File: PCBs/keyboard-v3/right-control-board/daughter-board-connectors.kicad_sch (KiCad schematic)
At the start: 0 parts

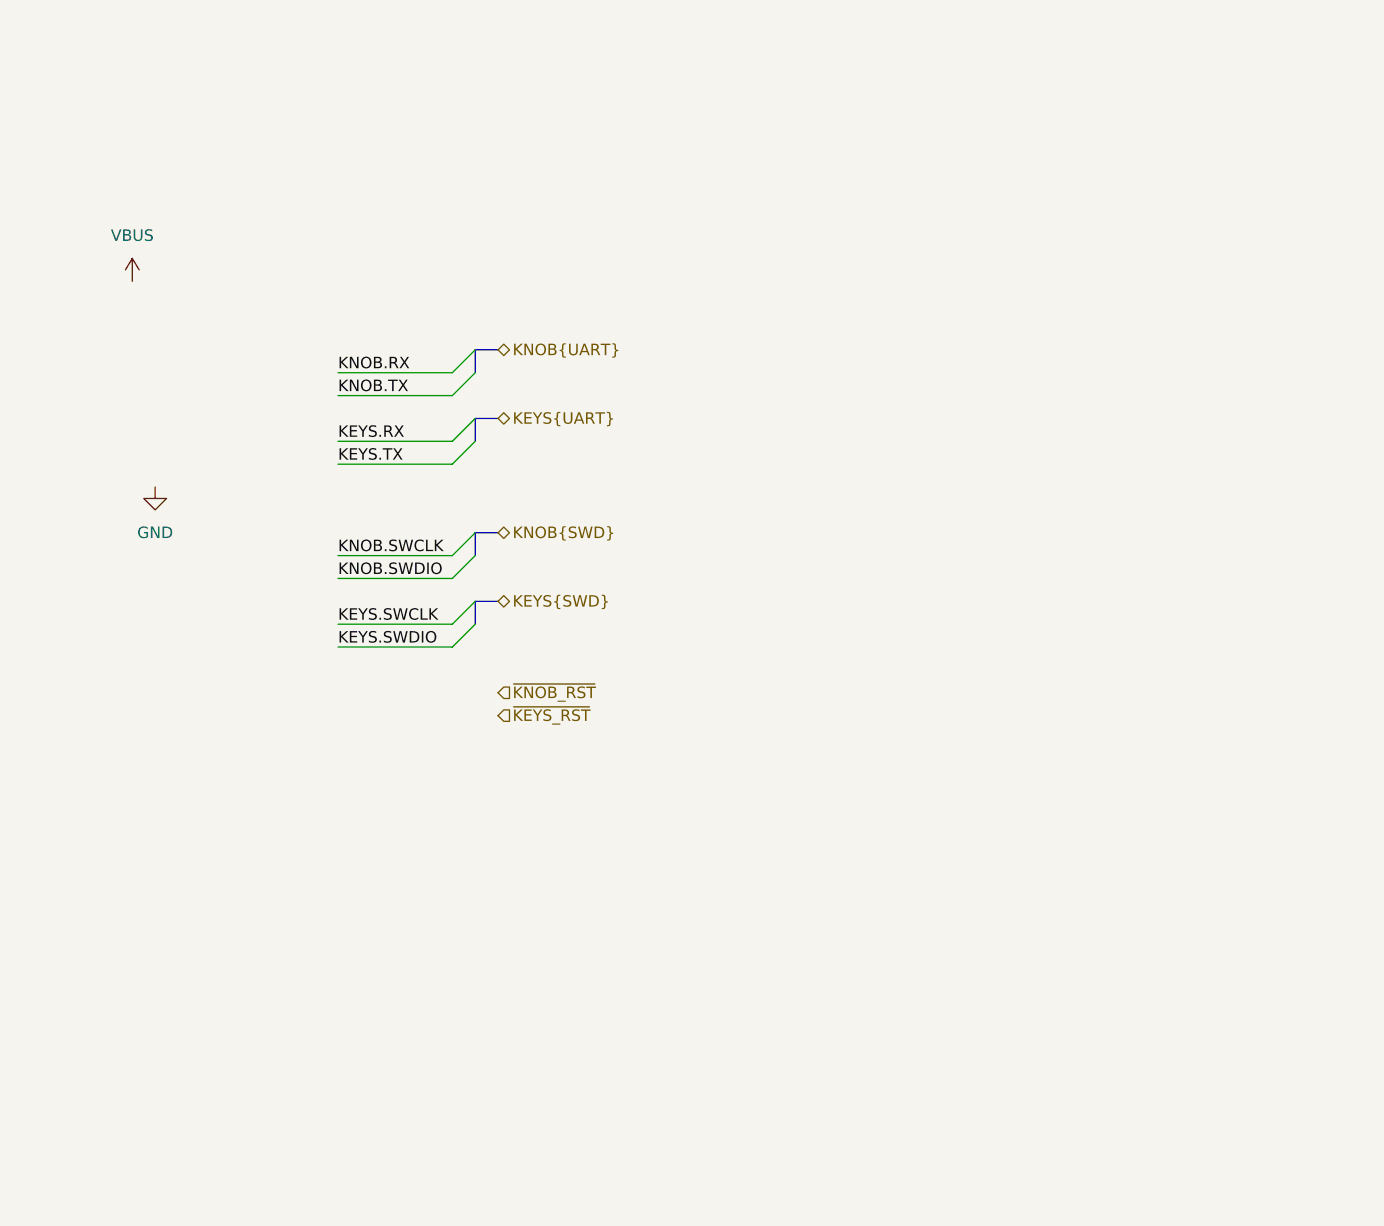
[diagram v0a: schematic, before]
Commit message: Key board schematic done and layout half done
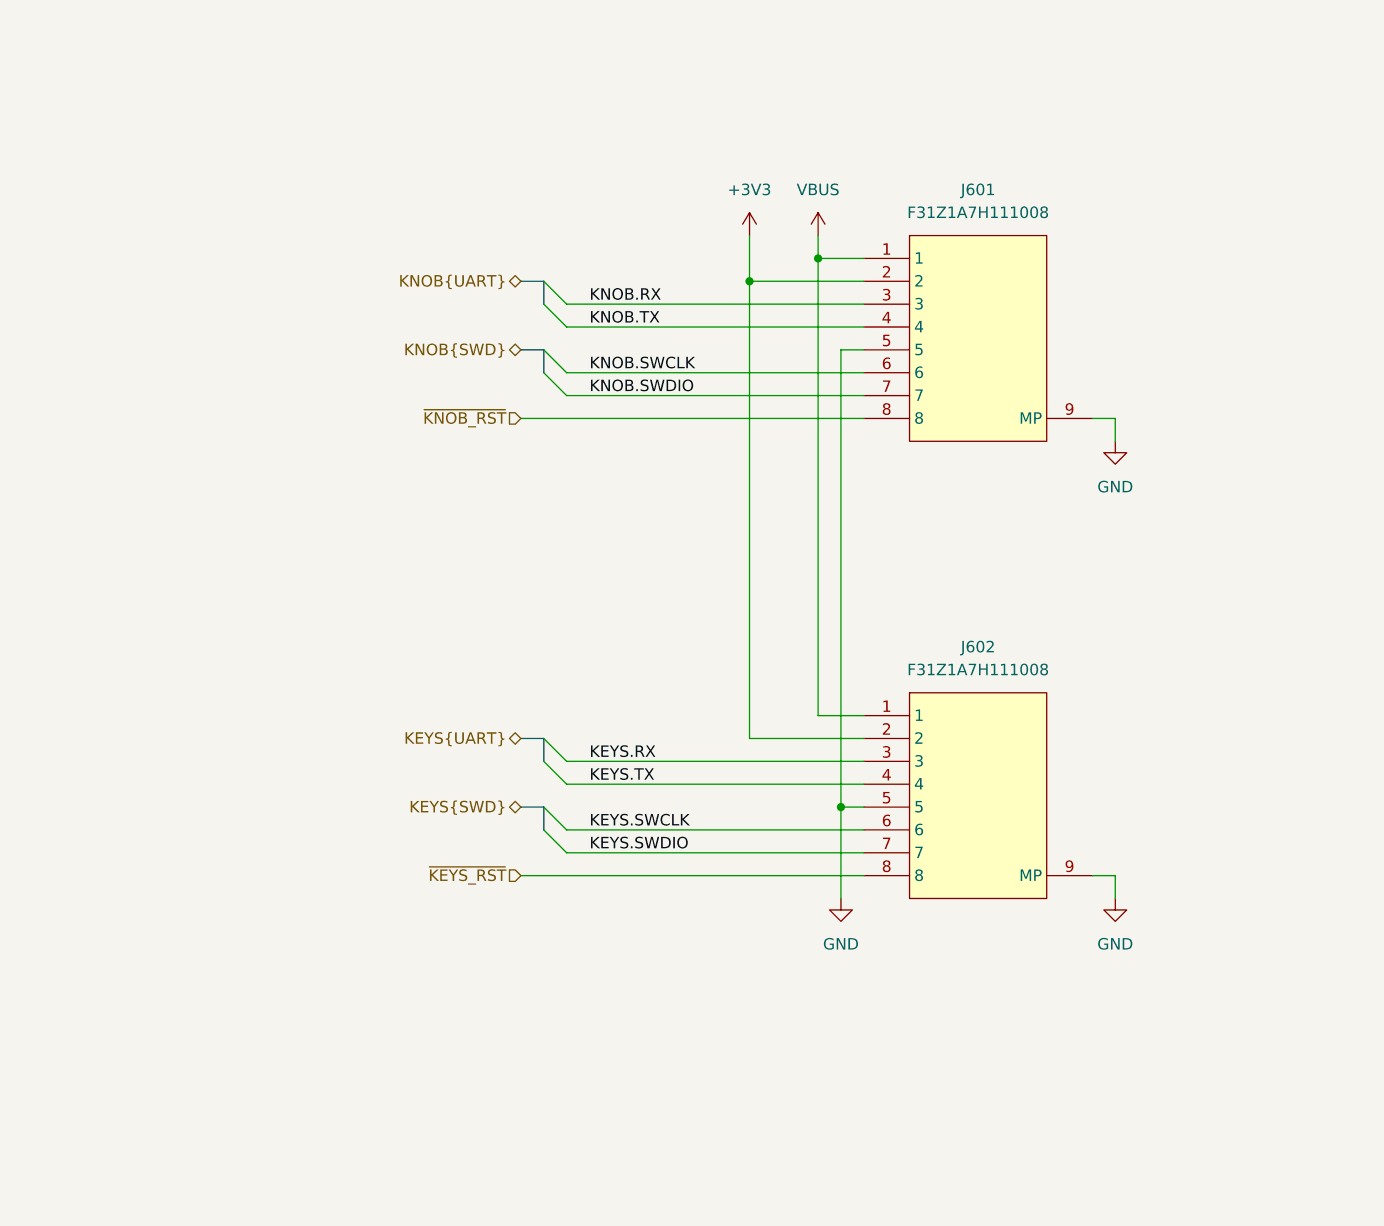
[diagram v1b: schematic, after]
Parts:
- added J601, J602: F31Z1A7H111008, project_footprints:F31Z1A7H111008, symbol CONN-FPC:F31Z1A7H111008
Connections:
- net GND: now also J601.10 (MP), J601.11 (MP), J601.12 (MP), J601.5, J601.9 (MP), J602.10 (MP), J602.11 (MP), J602.12 (MP), J602.5, J602.9 (MP)
- net KEYS.RX: now also J602.3
- net KEYS.SWCLK: now also J602.6
- net KEYS.SWDIO: now also J602.7
- net KEYS.TX: now also J602.4
- net KNOB.RX: now also J601.3
- net KNOB.SWCLK: now also J601.6
- net KNOB.SWDIO: now also J601.7
- net KNOB.TX: now also J601.4
- net VBUS: now also J601.1, J602.1
- net ~{KEYS_RST}: now also J602.8
- net ~{KNOB_RST}: now also J601.8
- new net +3V3: J601.2, J602.2

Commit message: Added debug-breakout board, progress on right side schematics & layout
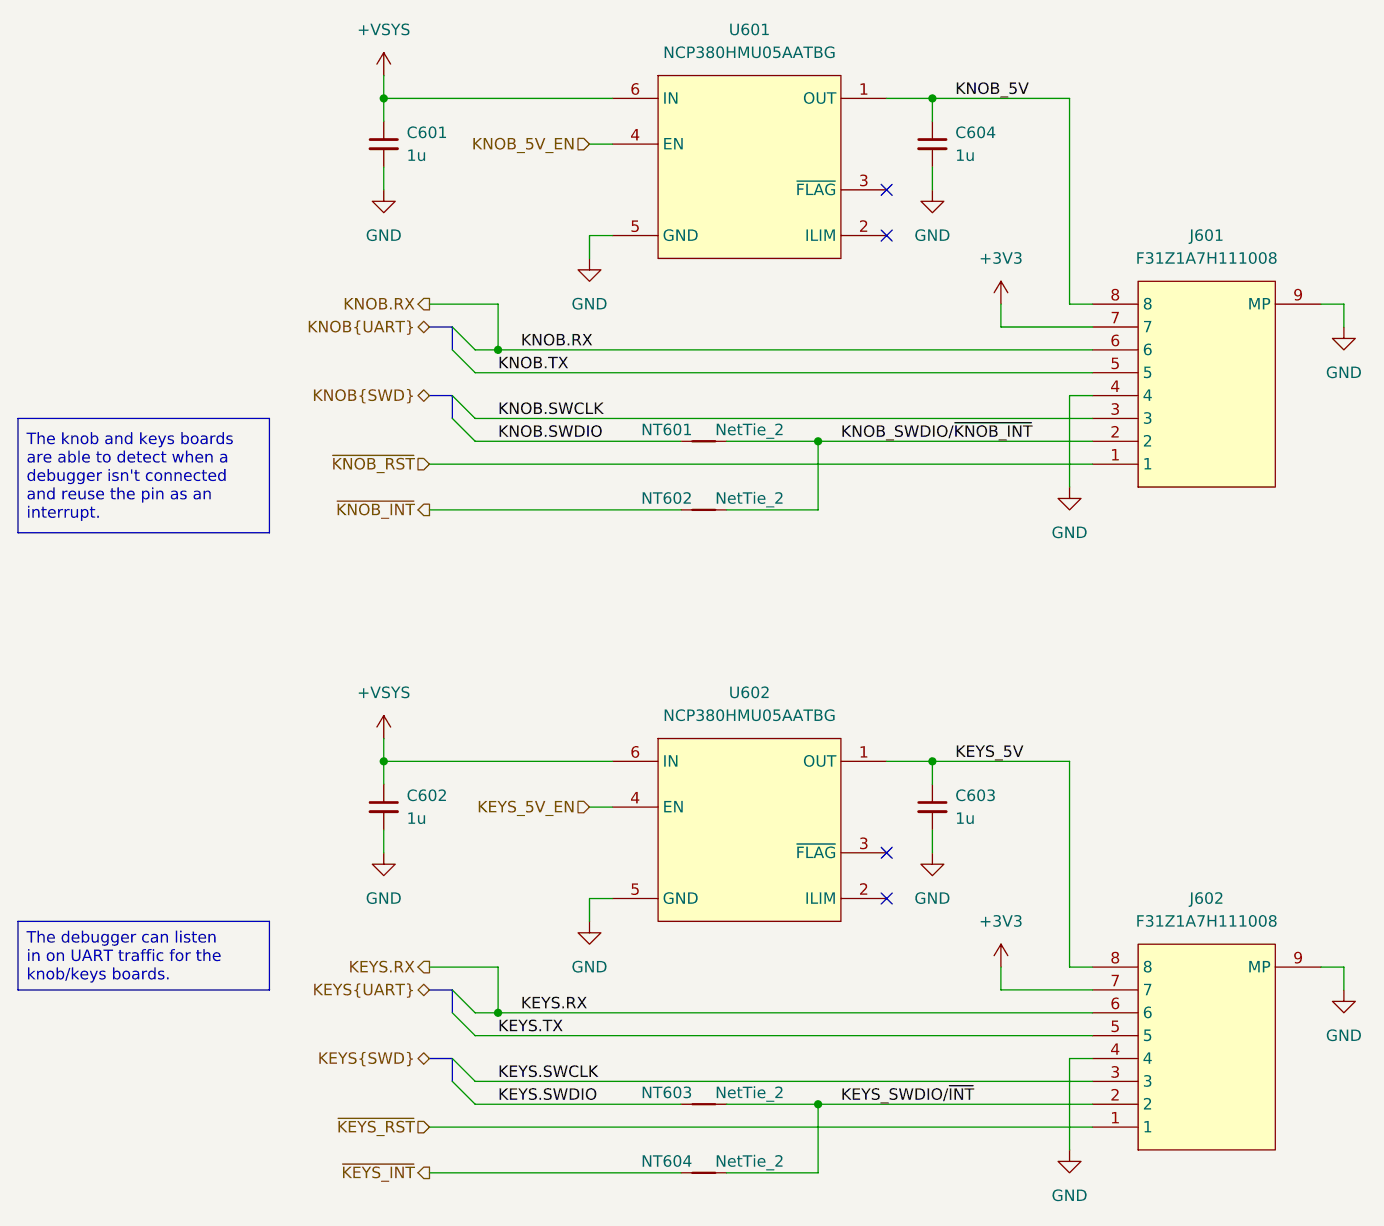
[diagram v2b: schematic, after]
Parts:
- added C601, C602, C603, C604: 1u, project_footprints:C_0402, symbol DEV:C_SMALL
- added NT601, NT602, NT603, NT604: NetTie_2, project_footprints:NetTie-2_SMD_Pad0.15mm, symbol Device:NetTie_2
- added U601, U602: NCP380HMU05AATBG, project_footprints:SON65P200X200X55-7N, symbol PWR-SWCH:NCP380HMU05AATBG
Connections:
- net +3V3: now also J601.7, J602.7; no longer J601.2, J602.2
- net GND: now also J601.4, J602.4, C601.2, C602.2, C603.2, C604.2, U601.5 (GND), U601.7 (GND), U602.5 (GND), U602.7 (GND); no longer J601.5, J602.5
- net KEYS.RX: now also J602.6; no longer J602.3
- net KEYS.SWCLK: now also J602.3; no longer J602.6
- net KEYS.SWDIO: now also NT603.1; no longer J602.7
- net KEYS.TX: now also J602.5; no longer J602.4
- net KNOB.RX: now also J601.6; no longer J601.3
- net KNOB.SWCLK: now also J601.3; no longer J601.6
- net KNOB.SWDIO: now also NT601.1; no longer J601.7
- net KNOB.TX: now also J601.5; no longer J601.4
- net ~{KEYS_RST}: now also J602.1; no longer J602.8
- net ~{KNOB_RST}: now also J601.1; no longer J601.8
- removed net VBUS: J601.1, J602.1
- new net +VSYS: C601.1, C602.1, U601.6 (IN), U602.6 (IN)
- new net KEYS_5V: C603.1, J602.8, U602.1 (OUT)
- new net KEYS_5V_EN: U602.4 (EN)
- new net KEYS_SWDIO/~{INT}: J602.2, NT603.2, NT604.2
- new net KNOB_5V: C604.1, J601.8, U601.1 (OUT)
- new net KNOB_5V_EN: U601.4 (EN)
- new net KNOB_SWDIO/~{KNOB_INT}: J601.2, NT601.2, NT602.2
- new net ~{KEYS_INT}: NT604.1
- new net ~{KNOB_INT}: NT602.1
- no-connect marks 0 -> 4
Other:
- moved on the sheet: J601, J602

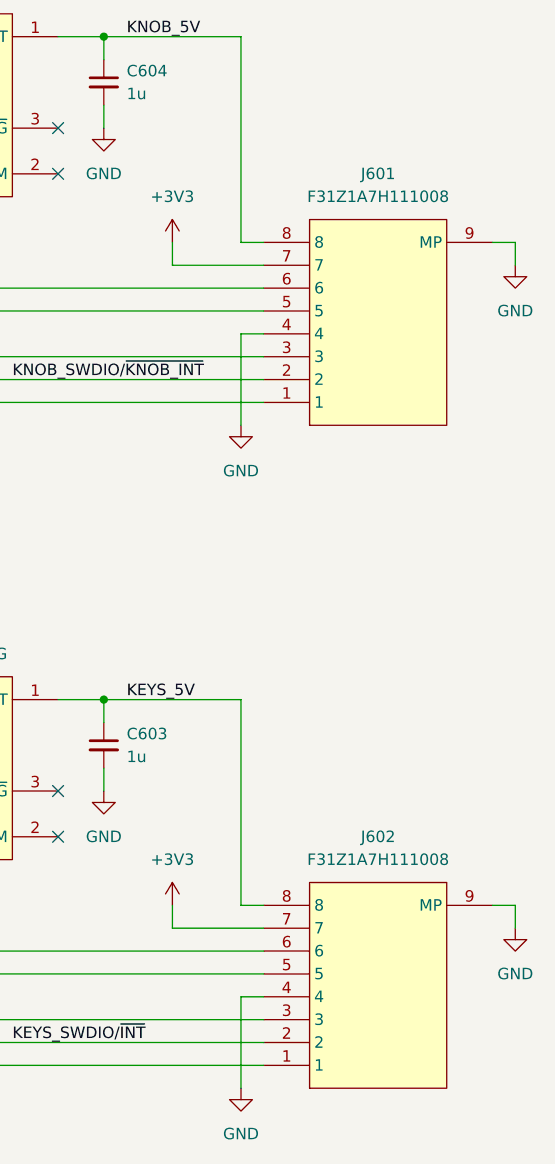
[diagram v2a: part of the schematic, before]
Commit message: Right control board placement and schematic done
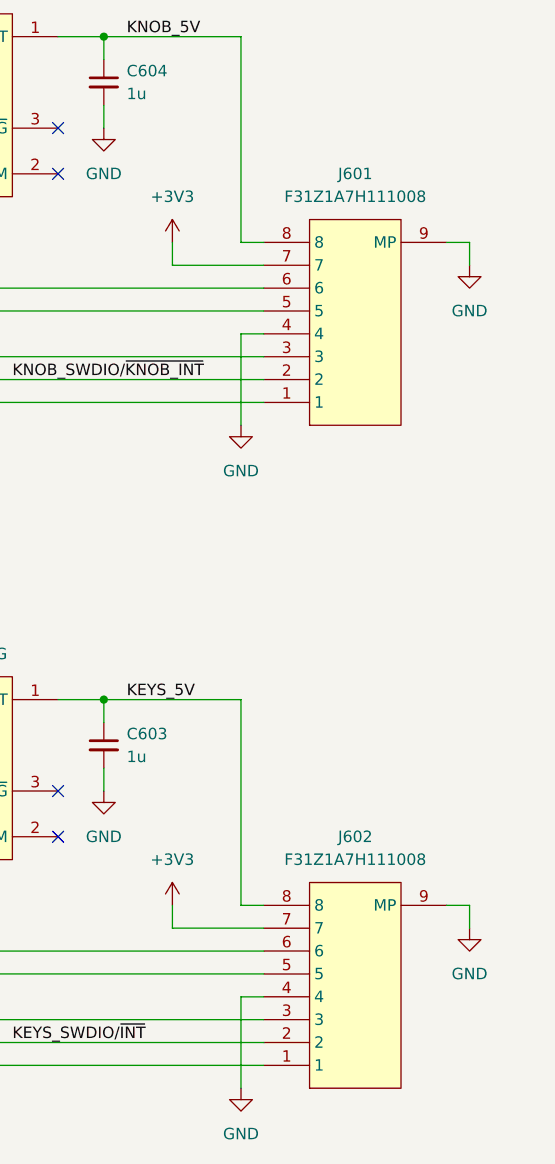
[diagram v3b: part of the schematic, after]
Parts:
- J601, J602: symbol CONN-FPC:F31Z1A7H111008 -> CONN-FPC:F31Z-1A7H1-11008
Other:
- moved on the sheet: J601, J602
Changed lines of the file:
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@@
 	(wire
 		(pts
-			(xy 218.44 58.42) (xy 218.44 60.96)
+			(xy 213.36 58.42) (xy 213.36 60.96)
 		)
 		(stroke
@@
 	(wire
 		(pts
-			(xy 215.9 58.42) (xy 218.44 58.42)
+			(xy 210.82 58.42) (xy 213.36 58.42)
 		)
 		(stroke
@@
 	(wire
 		(pts
-			(xy 215.9 132.08) (xy 218.44 132.08)
+			(xy 210.82 132.08) (xy 213.36 132.08)
 		)
 		(stroke
@@
 	(wire
 		(pts
-			(xy 218.44 134.62) (xy 218.44 132.08)
+			(xy 213.36 134.62) (xy 213.36 132.08)
 		)
 		(stroke
@@
 	(symbol
 		(lib_id "power:GND")
-		(at 218.44 60.96 0)
+		(at 213.36 60.96 0)
 		(unit 1)
 		(exclude_from_sim no)
@@
 		(fields_autoplaced yes)
 		(property "Reference" "#PWR0603"
-			(at 218.44 67.31 0)
+			(at 213.36 67.31 0)
 			(effects
 				(font
@@
 		)
 		(property "Value" "GND"
-			(at 218.44 66.04 0)
+			(at 213.36 66.04 0)
 			(effects
 				(font
@@
 		)
 		(property "Footprint" ""
-			(at 218.44 60.96 0)
+			(at 213.36 60.96 0)
 			(effects
 				(font
@@
 		)
 		(property "Datasheet" ""
-			(at 218.44 60.96 0)
+			(at 213.36 60.96 0)
 			(effects
 				(font
@@
 		)
 		(property "Description" ""
-			(at 218.44 60.96 0)
+			(at 213.36 60.96 0)
 			(effects
 				(font
@@
 	)
 	(symbol
-		(lib_id "CONN-FPC:F31Z1A7H111008")
-		(at 203.2 78.74 0)
+		(lib_id "CONN-FPC:F31Z-1A7H1-11008")
+		(at 200.66 78.74 0)
 		(mirror x)
 		(unit 1)
@@
 		(dnp no)
 		(property "Reference" "J601"
-			(at 203.2 50.8 0)
+			(at 200.66 50.8 0)
 			(effects
 				(font
@@
 		)
 		(property "Value" "F31Z1A7H111008"
-			(at 203.2 53.34 0)
+			(at 200.66 53.34 0)
 			(effects
 				(font
@@
 		)
 		(property "Footprint" "project_footprints:F31Z1A7H111008"
-			(at 203.2 50.8 0)
+			(at 200.66 50.8 0)
 			(effects
 				(font
@@
 		)
 		(property "Datasheet" "https://cdn.amphenol-cs.com/media/wysiwyg/files/drawing/f31z-f31w.pdf"
-			(at 203.2 48.26 0)
+			(at 200.66 48.26 0)
 			(effects
 				(font
@@
 		)
 		(property "Description" "Flex Connector, 0.50mm Pitch, Height 4.25mm, Vertical, Slider type, ZIF, 8 position, With MYLAR"
-			(at 203.2 53.34 0)
+			(at 200.66 53.34 0)
 			(effects
 				(font
@@
 		)
 		(property "Height" "4.45"
-			(at 203.2 45.72 0)
+			(at 200.66 45.72 0)
 			(effects
 				(font
@@
 	)
 	(symbol
-		(lib_id "CONN-FPC:F31Z1A7H111008")
-		(at 203.2 152.4 0)
+		(lib_id "CONN-FPC:F31Z-1A7H1-11008")
+		(at 200.66 152.4 0)
 		(mirror x)
 		(unit 1)
@@
 		(dnp no)
 		(property "Reference" "J602"
-			(at 203.2 124.46 0)
+			(at 200.66 124.46 0)
 			(effects
 				(font
@@
 		)
 		(property "Value" "F31Z1A7H111008"
-			(at 203.2 127 0)
+			(at 200.66 127 0)
 			(effects
 				(font
@@
 		)
 		(property "Footprint" "project_footprints:F31Z1A7H111008"
-			(at 203.2 124.46 0)
+			(at 200.66 124.46 0)
 			(effects
 				(font
@@
 		)
 		(property "Datasheet" "https://cdn.amphenol-cs.com/media/wysiwyg/files/drawing/f31z-f31w.pdf"
-			(at 203.2 121.92 0)
+			(at 200.66 121.92 0)
 			(effects
 				(font
@@
 		)
 		(property "Description" "Flex Connector, 0.50mm Pitch, Height 4.25mm, Vertical, Slider type, ZIF, 8 position, With MYLAR"
-			(at 203.2 127 0)
+			(at 200.66 127 0)
 			(effects
 				(font
@@
 		)
 		(property "Height" "4.45"
-			(at 203.2 119.38 0)
+			(at 200.66 119.38 0)
 			(effects
 				(font
@@
 	(symbol
 		(lib_id "power:GND")
-		(at 218.44 134.62 0)
+		(at 213.36 134.62 0)
 		(unit 1)
 		(exclude_from_sim no)
@@
 		(fields_autoplaced yes)
 		(property "Reference" "#PWR0602"
-			(at 218.44 140.97 0)
+			(at 213.36 140.97 0)
 			(effects
 				(font
@@
 		)
 		(property "Value" "GND"
-			(at 218.44 139.7 0)
+			(at 213.36 139.7 0)
 			(effects
 				(font
@@
 		)
 		(property "Footprint" ""
-			(at 218.44 134.62 0)
+			(at 213.36 134.62 0)
 			(effects
 				(font
@@
 		)
 		(property "Datasheet" ""
-			(at 218.44 134.62 0)
+			(at 213.36 134.62 0)
 			(effects
 				(font
@@
 		)
 		(property "Description" ""
-			(at 218.44 134.62 0)
-			(effects
-				(font
+			(at 213.36 134.62 0)
+			(effects
+				(font
